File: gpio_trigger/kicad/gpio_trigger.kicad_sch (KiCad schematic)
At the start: 21 parts, among them J1 TRS_CAM_A, J2 TRS_CAM_B, J3 Pi_GPIO, U1 4N35, U2 4N35, U3 4N35, U4 4N35

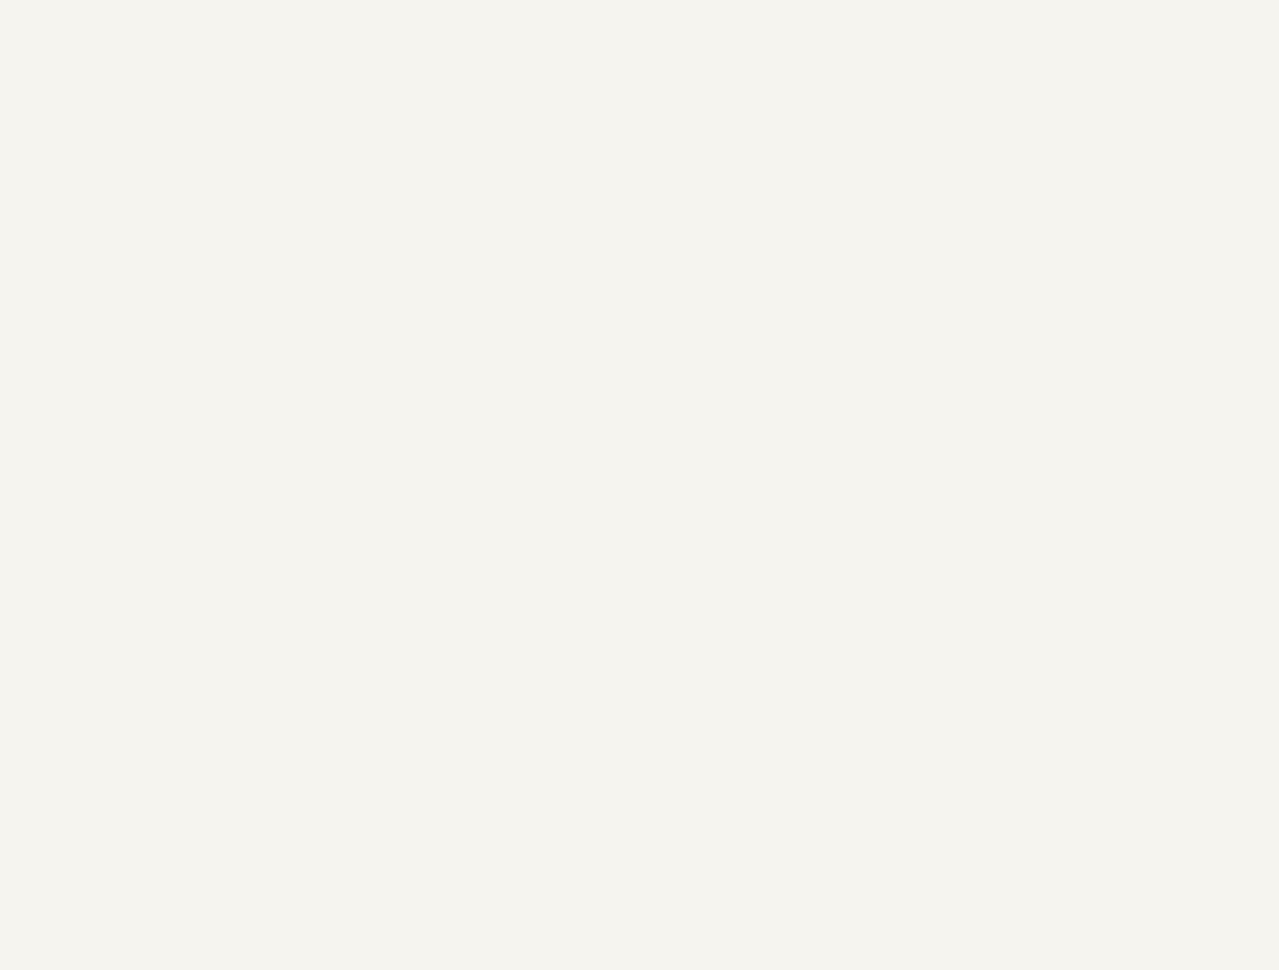
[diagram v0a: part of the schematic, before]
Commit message: Pulse focus and shutter on both camera jacks from the Pi GPIO header.
BCM 20 and 26 hold focus while BCM 21 and 19 release, so either jumper position fires, and libgpiod 2 drops the lines with release() after the pulse.

Co-authored-by: Cursor <cursoragent@cursor.com>
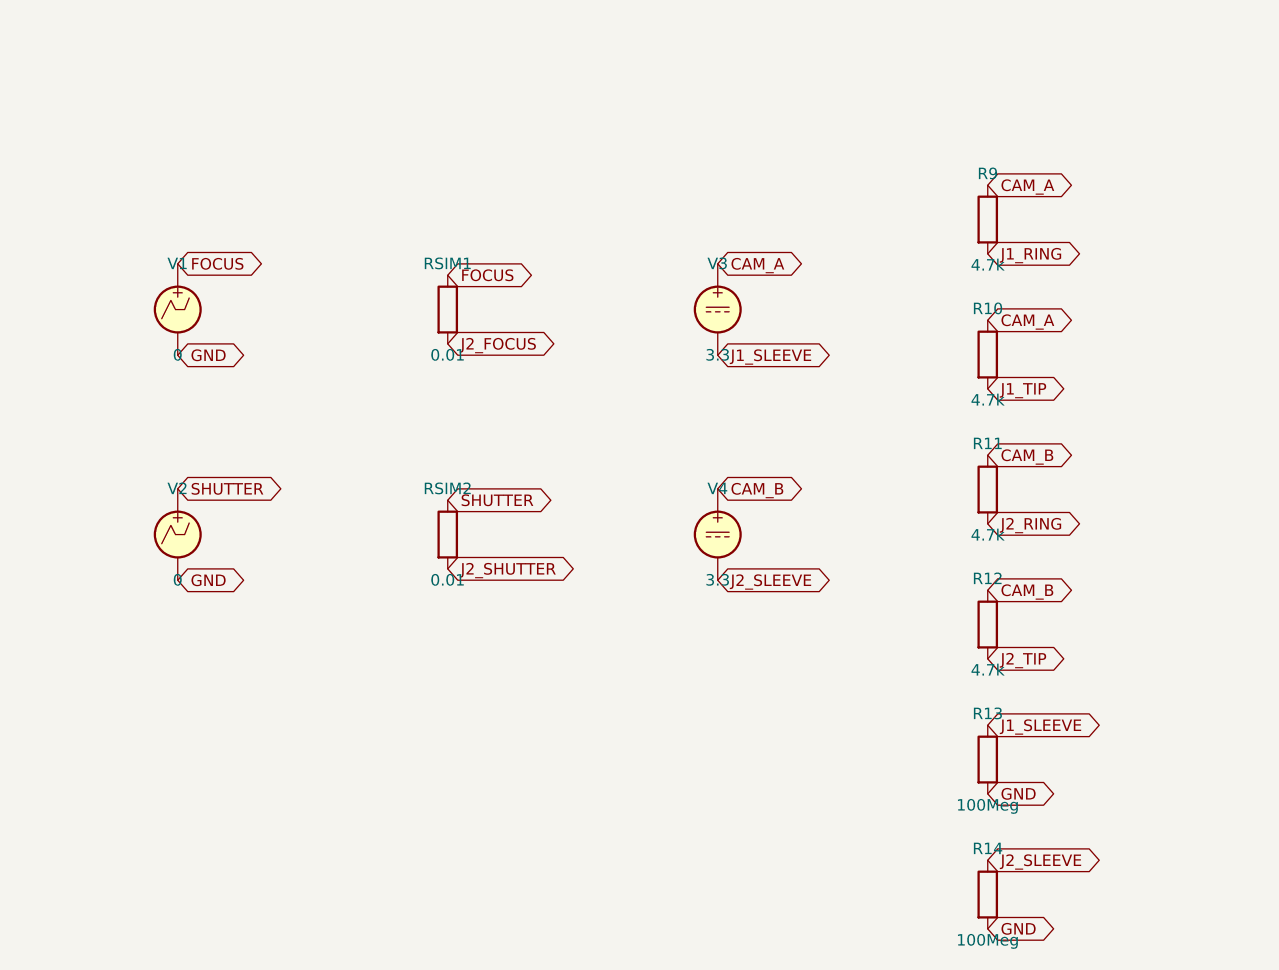
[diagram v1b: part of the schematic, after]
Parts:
- added R10, R11, R12, R9: 4.7k, symbol Device:R
- added R13, R14: 100Meg, symbol Device:R
- added RSIM1, RSIM2: 0.01, symbol Device:R
- added V1, V2: 0, symbol Simulation_SPICE:VPWL
- added V3, V4: 3.3, symbol Simulation_SPICE:VDC
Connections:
- net FOCUS: now also RSIM1.1, V1.1
- net GND: now also R13.2, R14.2, V1.2, V2.2
- net J1_RING: now also R9.2
- net J1_SLEEVE: now also R13.1, V3.2
- net J1_TIP: now also R10.2
- net J2_FOCUS: now also RSIM1.2
- net J2_RING: now also R11.2
- net J2_SHUTTER: now also RSIM2.2
- net J2_SLEEVE: now also R14.1, V4.2
- net J2_TIP: now also R12.2
- net SHUTTER: now also RSIM2.1, V2.1
- new net CAM_A: R10.1, R9.1, V3.1
- new net CAM_B: R11.1, R12.1, V4.1
